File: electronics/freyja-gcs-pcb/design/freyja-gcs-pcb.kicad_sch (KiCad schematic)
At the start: 35 parts, among them J1 Conn_01x07_Pin, J2 GT-USB-7010ASV, J8 JST SH, J9 JST SH, SW1 SW_SPST, SW2 SW_SPST, U1 SN65HVD232DR, U2 STM32U575RGTx, Y1 48MHz, Y2 32768Hz

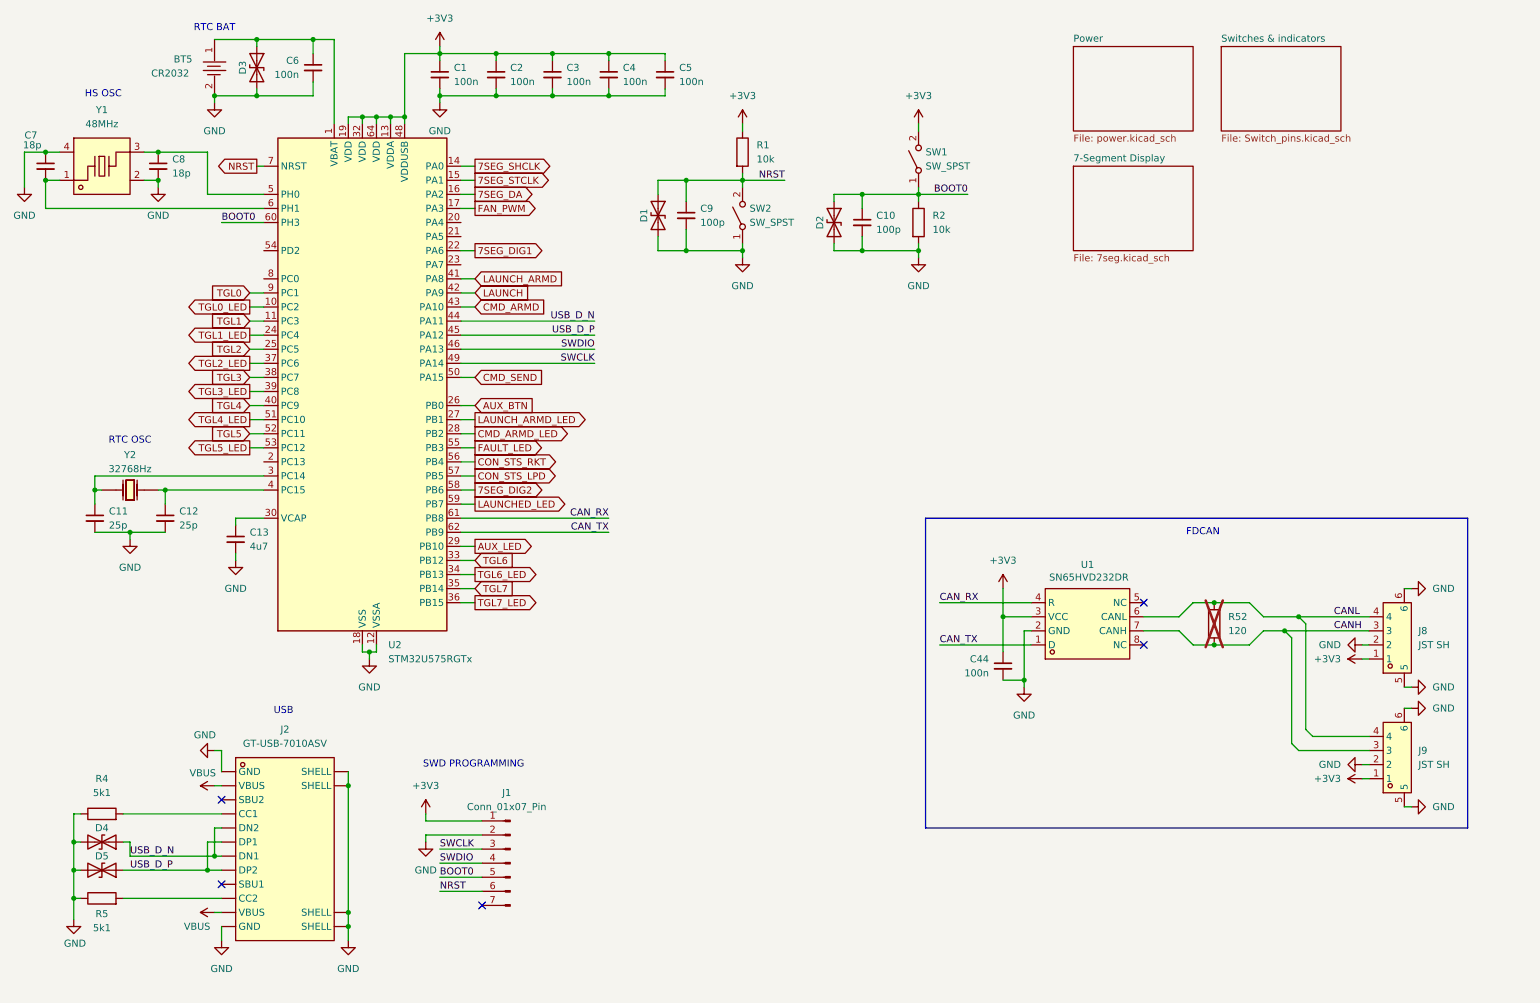
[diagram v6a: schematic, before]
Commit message: more esd diodes
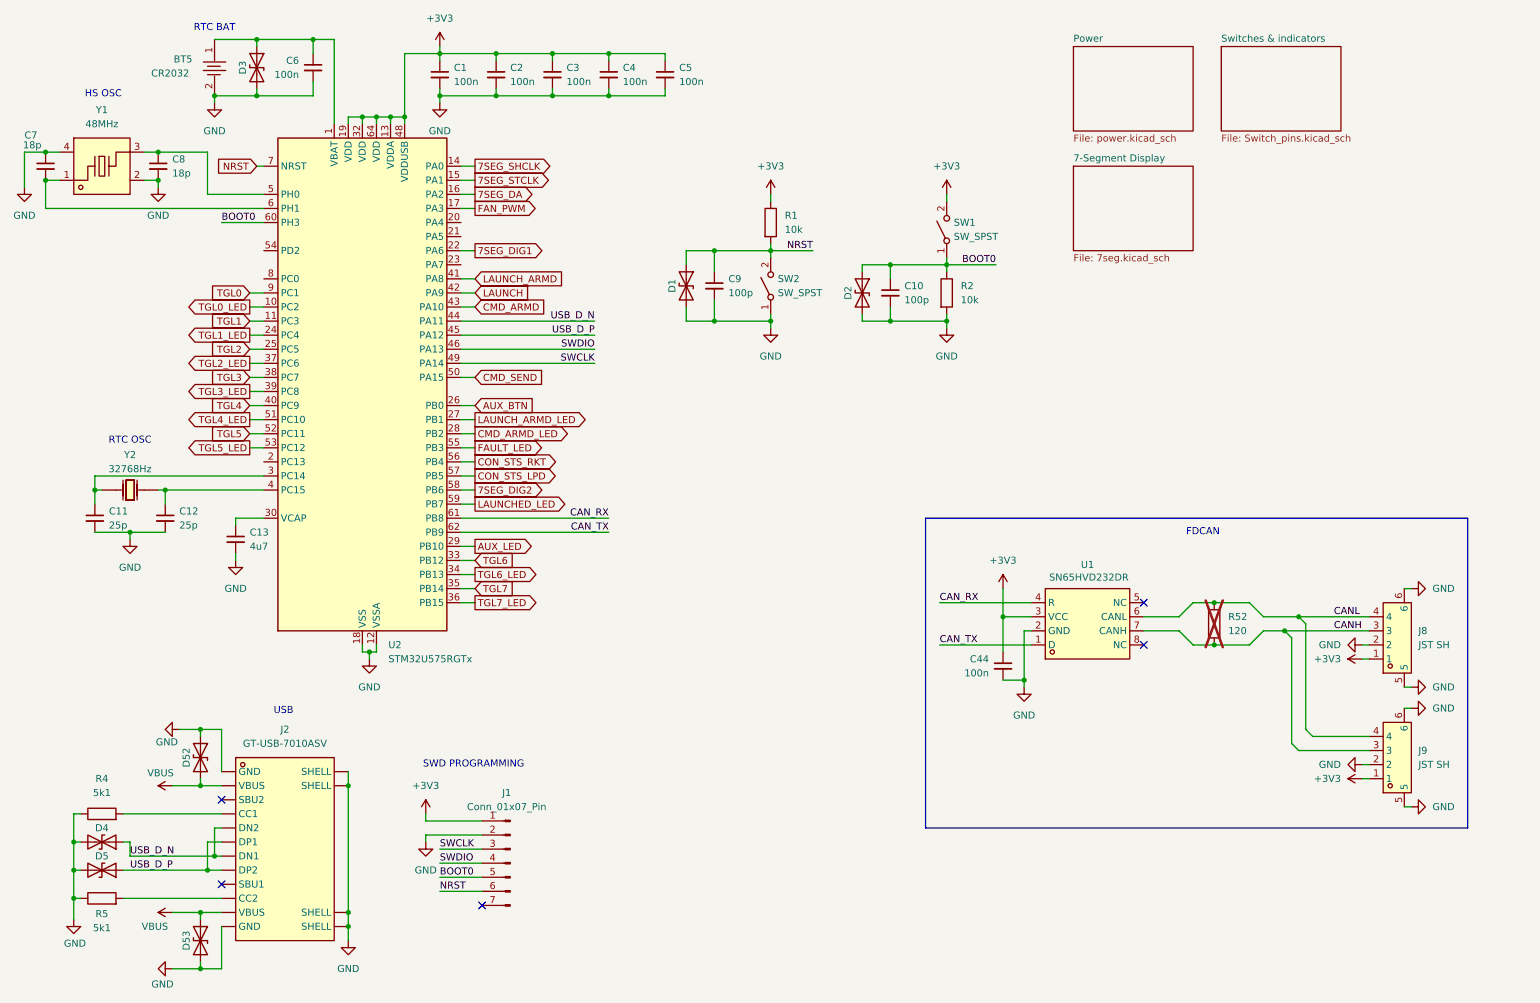
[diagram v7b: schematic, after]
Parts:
- added D52, D53: 0603ESDA-05N, Diode_SMD:D_0603_1608Metric_Pad1.05x0.95mm_HandSolder, symbol Device:D_TVS
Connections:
- net GND: now also D52.1 (A1), D53.2 (A2)
- net VBUS: now also D52.2 (A2), D53.1 (A1)
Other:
- moved on the sheet: C10, C9, D1, D2, R1, R2, SW1, SW2

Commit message: more esd diodes!
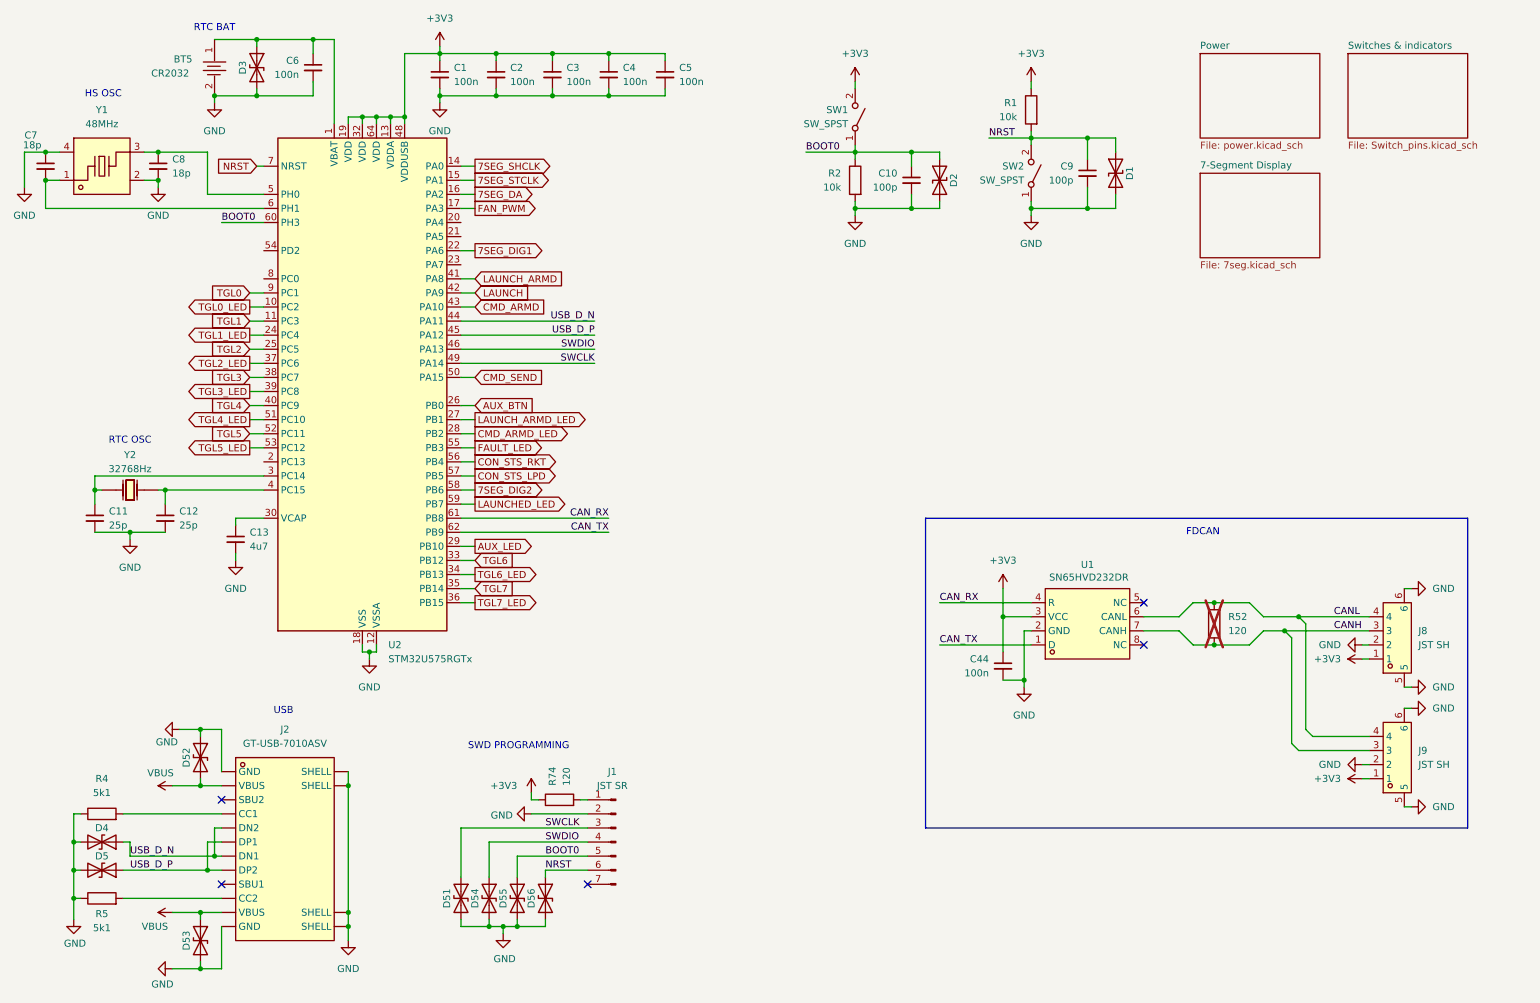
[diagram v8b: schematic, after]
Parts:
- added D51, D54, D55, D56: 0603ESDA-05N, Diode_SMD:D_0603_1608Metric_Pad1.05x0.95mm_HandSolder, symbol Device:D_TVS
- added R74: 120, symbol Device:R
- J1: value Conn_01x07_Pin -> JST SR
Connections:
- net +3V3: now also R74.1; no longer J1.1 (Pin_1)
- net BOOT0: now also D55.1 (A1)
- net GND: now also D51.2 (A2), D54.2 (A2), D55.2 (A2), D56.2 (A2)
- net NRST: now also D56.1 (A1)
- net SWCLK: now also D51.1 (A1)
- net SWDIO: now also D54.1 (A1)
- new net: J1.1 (Pin_1), R74.2
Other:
- moved on the sheet: C10, C9, D1, D2, J1, R1, R2, SW1, SW2
